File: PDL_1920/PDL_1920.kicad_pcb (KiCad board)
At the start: 4 copper layers, 75.8 x 76.2 mm, 100 parts, among them IC1 FAN4010IL6X_F113, IC2 FAN4010IL6X_F113, IC3 FAN4010IL6X_F113, J1 SC_19-20, J2 Conn_01x06, J3 47219-2001, U1 STMPS2141STR, U2 STMPS2141STR, U3 PIC32MM0256GPM028T, U4 TXB0104PWR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

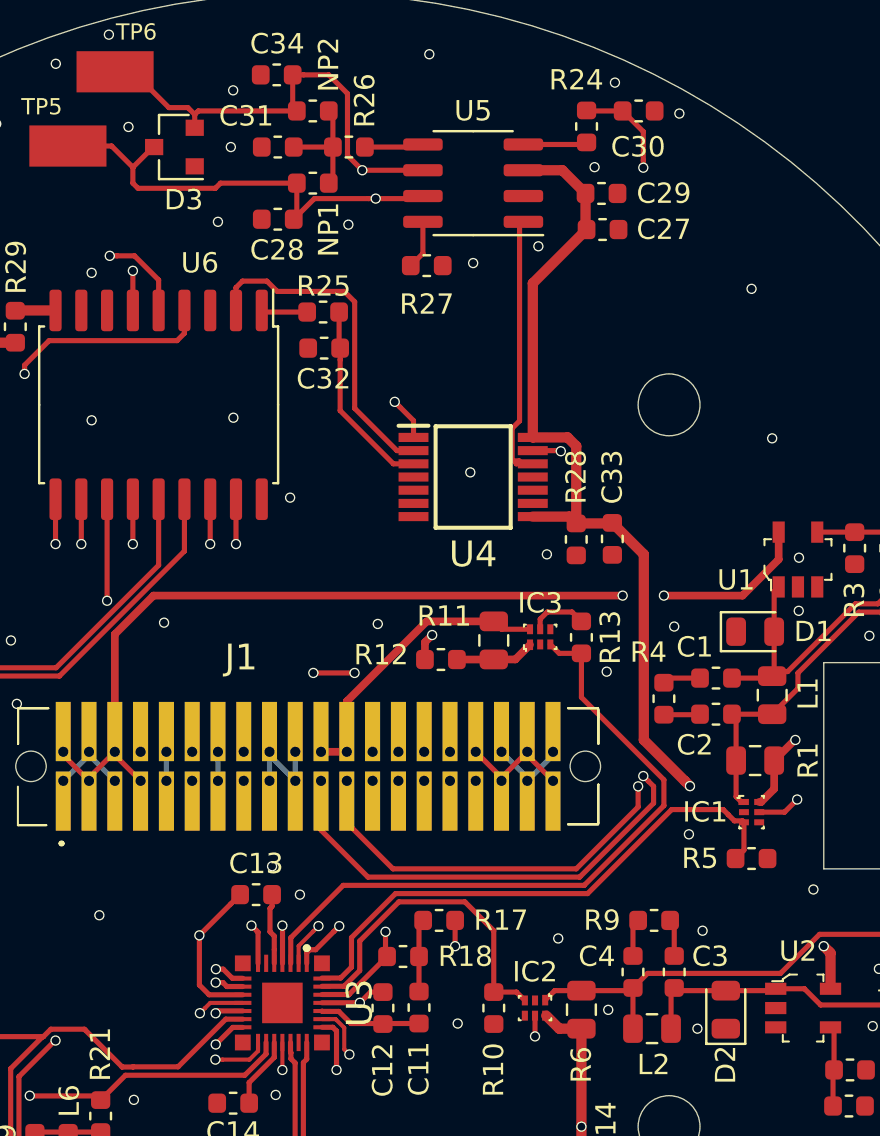
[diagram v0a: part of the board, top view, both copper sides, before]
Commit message: Clearance changes
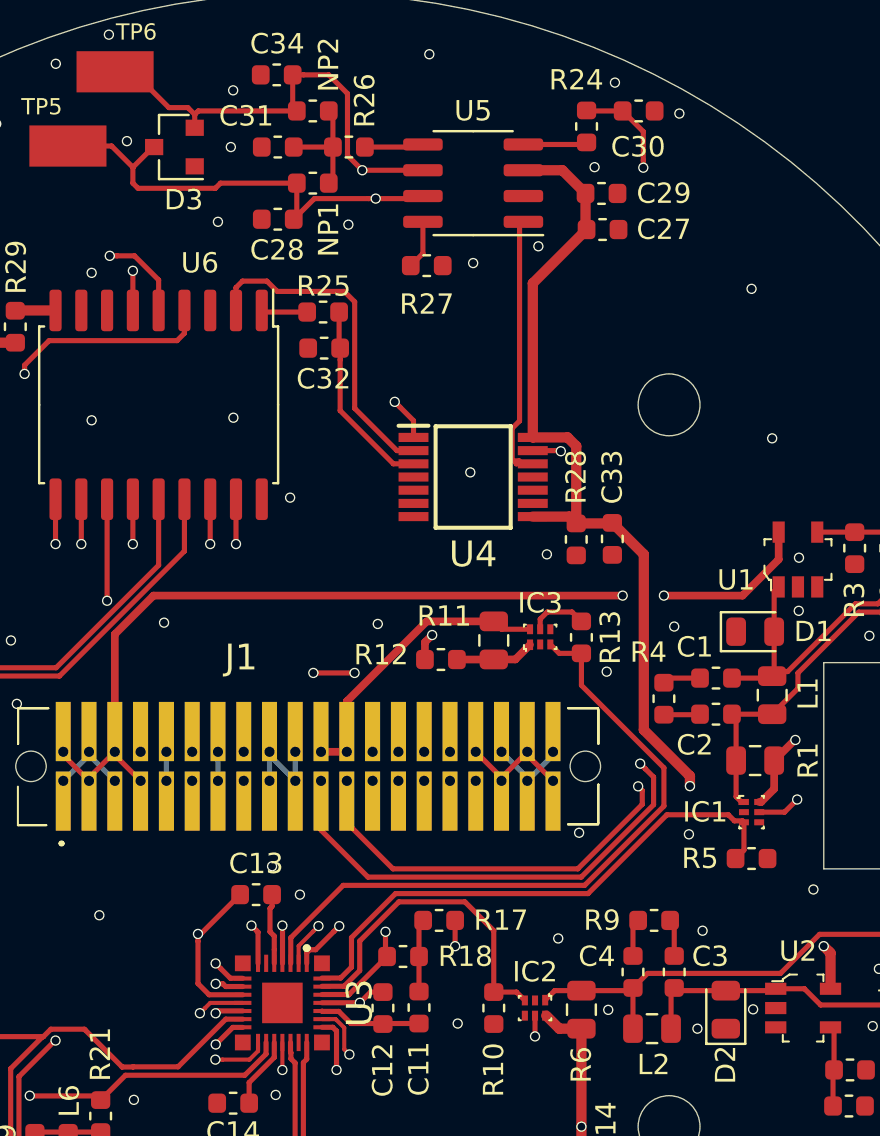
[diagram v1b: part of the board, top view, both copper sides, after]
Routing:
- net CAN_H: track 80.4 -> 79.6 mm
- net CAN_L: track 79.0 -> 78.4 mm
- net GND: vias 86 -> 88
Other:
- board text added: "Pressure Data Logger Hannah Imboden 2019 -2020"
- board text removed: "Pressure Data Logger 2019 -2020"
